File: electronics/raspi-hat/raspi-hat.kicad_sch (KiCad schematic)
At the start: 15 parts, among them J1 Raspberry Pi 40-Pin, J2 24V, J3 12V to other boards, J4 CAN, J5 5V to other boards, Q1 DMG2305UX-13, U1 MCP2515-xSO, U2 MAX33012EASA+, U3 DMMT5401-7-F, Y1 Crystal_GND24_Small

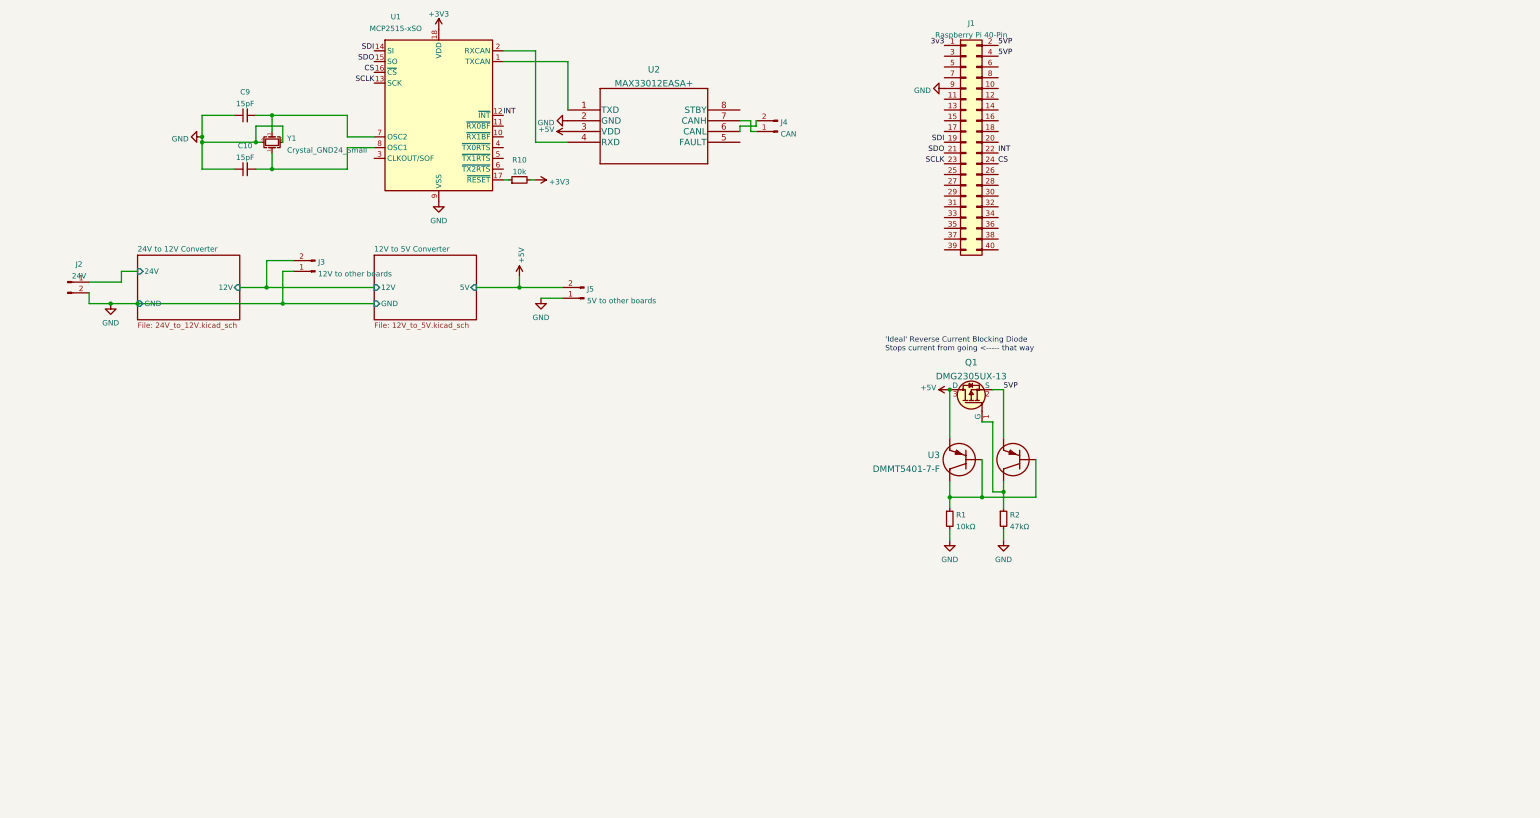
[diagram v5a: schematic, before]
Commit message: Finish designing raspi hat
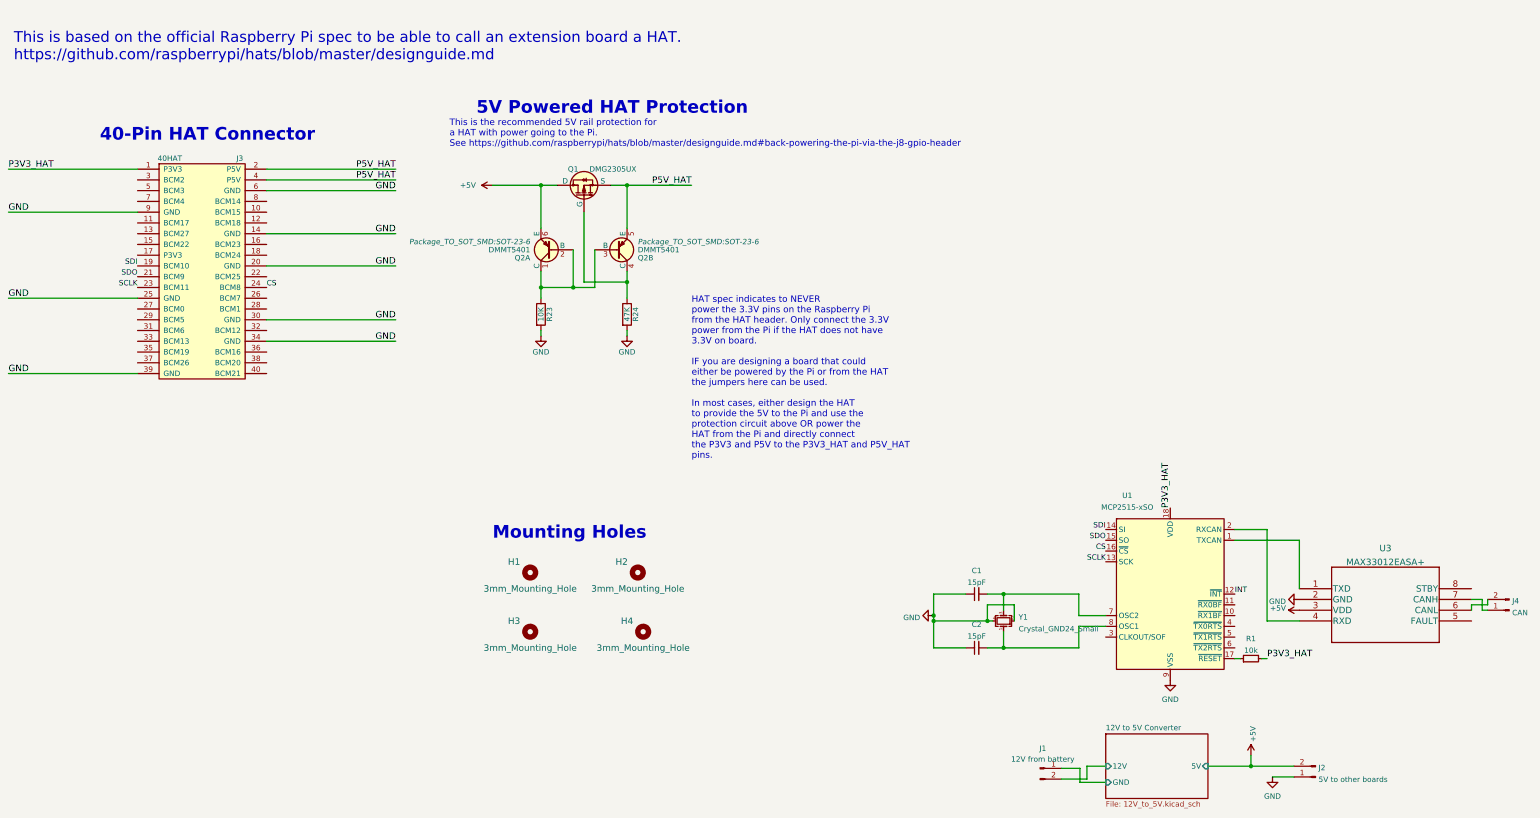
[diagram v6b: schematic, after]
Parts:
- removed C10, C9: 15pF, Capacitor_SMD:C_0603_1608Metric, symbol Device:C_Small
- removed J1: Raspberry Pi 40-Pin, Connector_PinHeader_2.54mm:PinHeader_2x20_P2.54mm_Vertical, symbol Connector_Generic:Conn_02x20_Odd_Even
- removed J3: 12V to other boards, Custom Footprints:PowerPoleThroughHole, symbol Connector:Conn_01x02_Male
- removed J5: 5V to other boards, Custom Footprints:LatchingConnector2POS, symbol Connector:Conn_01x02_Male
- removed Q1: DMG2305UX-13, digikey-footprints:SOT-23-3, symbol dk_Transistors-FETs-MOSFETs-Single:DMG2305UX-13
- removed R10: 10k, Resistor_SMD:R_0603_1608Metric, symbol Device:R_Small
- removed R2: 47kΩ, Resistor_SMD:R_0603_1608Metric, symbol Device:R_Small
- removed U2: MAX33012EASA+, MAX33012EASA+:MAX33012EASA+, symbol MAX33012EASA+:MAX33012EASA+
- removed U3: DMMT5401-7-F, DMMT5401-7-F:DMMT5401-7-F, symbol DMMT5401-7-F:DMMT5401-7-F
- added C1, C2: 15pF, Capacitor_SMD:C_0603_1608Metric, symbol Device:C_Small
- added H1, H2, H3, H4: 3mm_Mounting_Hole, project_footprints:NPTH_3mm_ID, symbol Mechanical:MountingHole
- added J1: 12V from battery, Custom Footprints:PowerPoleThroughHole, symbol Connector:Conn_01x02_Male
- added J3: 40HAT, Connector_PinSocket_2.54mm:PinSocket_2x20_P2.54mm_Vertical, symbol raspberrypi_hat:OX40HAT
- added Q1: DMG2305UX, Package_TO_SOT_SMD:SOT-23, symbol raspberrypi_hat:DMG2305UX
- added Q2: DMMT5401, Package_TO_SOT_SMD:SOT-23-6, symbol raspberrypi_hat:DMMT5401
- added R23: 10K, Resistor_SMD:R_0603_1608Metric_Pad0.84x1.00mm_HandSolder, symbol Device:R
- added R24: 47K, Resistor_SMD:R_0603_1608Metric_Pad0.84x1.00mm_HandSolder, symbol Device:R
- added U3: MAX33012EASA+, MAX33012EASA+:MAX33012EASA+, symbol MAX33012EASA+:MAX33012EASA+
- J2: value 24V -> 5V to other boards; footprint Custom Footprints:PowerPoleThroughHole -> Custom Footprints:LatchingConnector2POS
- R1: value 10kΩ -> 10k
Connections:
- net 24V to 12V Converter/24V is gone; now on net GND: J2.1 (Pin_1)
- net +5V: now also J2.2 (Pin_2), Q1.3 (D), Q2.6 (E), U3.3 (VDD)
- net 12V to 5V Converter/12V: now also J1.2 (Pin_2)
- net CS: now also J3.24 (BCM8)
- net GND: now also C1.1, C2.1, J3.14 (GND), J3.20 (GND), J3.25 (GND), J3.30 (GND), J3.34 (GND), J3.39 (GND), J3.6 (GND), J3.9 (GND), R23.2, R24.2, U3.2 (GND); no longer J2.2 (Pin_2), R1.2
- net SCLK: now also J3.23 (BCM11)
- net SDI: now also J3.19 (BCM10)
- net SDO: now also J3.21 (BCM9)
- net at U1.8 (OSC1), Y1.1: now also C2.2
- net at R1.1: now also U1.17 (~{RESET})
- net at U1.1 (TXCAN): now also U3.1 (TXD)
- net at U1.2 (RXCAN): now also U3.4 (RXD)
- net at U1.7 (OSC2), Y1.3: now also C1.2
- net at J4.2 (Pin_2): now also U3.6 (CANL)
- net at J4.1 (Pin_1): now also U3.7 (CANH)
- net +3V3 renamed P3V3_HAT
- net P3V3_HAT: now also R1.2, J3.1 (P3V3)
- new net: Q1.1 (G), Q2.4 (C), R24.1
- new net: Q2.1 (C), Q2.2 (B), Q2.3 (B), R23.1
- new net 12V to 5V Converter/GND: J1.1 (Pin_1)
- new net P5V_HAT: J3.2 (P5V), J3.4 (P5V), Q1.2 (S), Q2.5 (E)
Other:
- removed sheet 24V to 12V Converter
- note added: "40-Pin HAT Connector"
- note added: "5V Powered HAT Protection"
- note added: "HAT spec indicates to NEVER power the 3.3V pins on the Raspberry Pi from the HAT header. Only connect the 3.3V power from the Pi if the HAT does not have 3.3V on board. IF you are designing a board that could either be powered by the Pi or from the HAT the jumpers here can be used. In most cases, either design the HAT to provide the 5V to the Pi and use the protection circuit above OR power the H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"
- note added: "Mounting Holes"
- note added: "This is based on the official Raspberry Pi spec to be able to call an extension board a HAT. https://github.com/raspberrypi/hats/blob/master/designguide.md"
- note added: "This is the recommended 5V rail protection for a HAT with power going to the Pi. See https://github.com/raspberrypi/hats/blob/master/designguide.md#back-powering-the-pi-via-the-j8-gpio-header"
- note removed: "'Ideal' Reverse Current Blocking Diode Stops current from going <----- that way"
- title: (none) -> Raspberry Pi HAT

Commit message: Update raspi HAT schematic
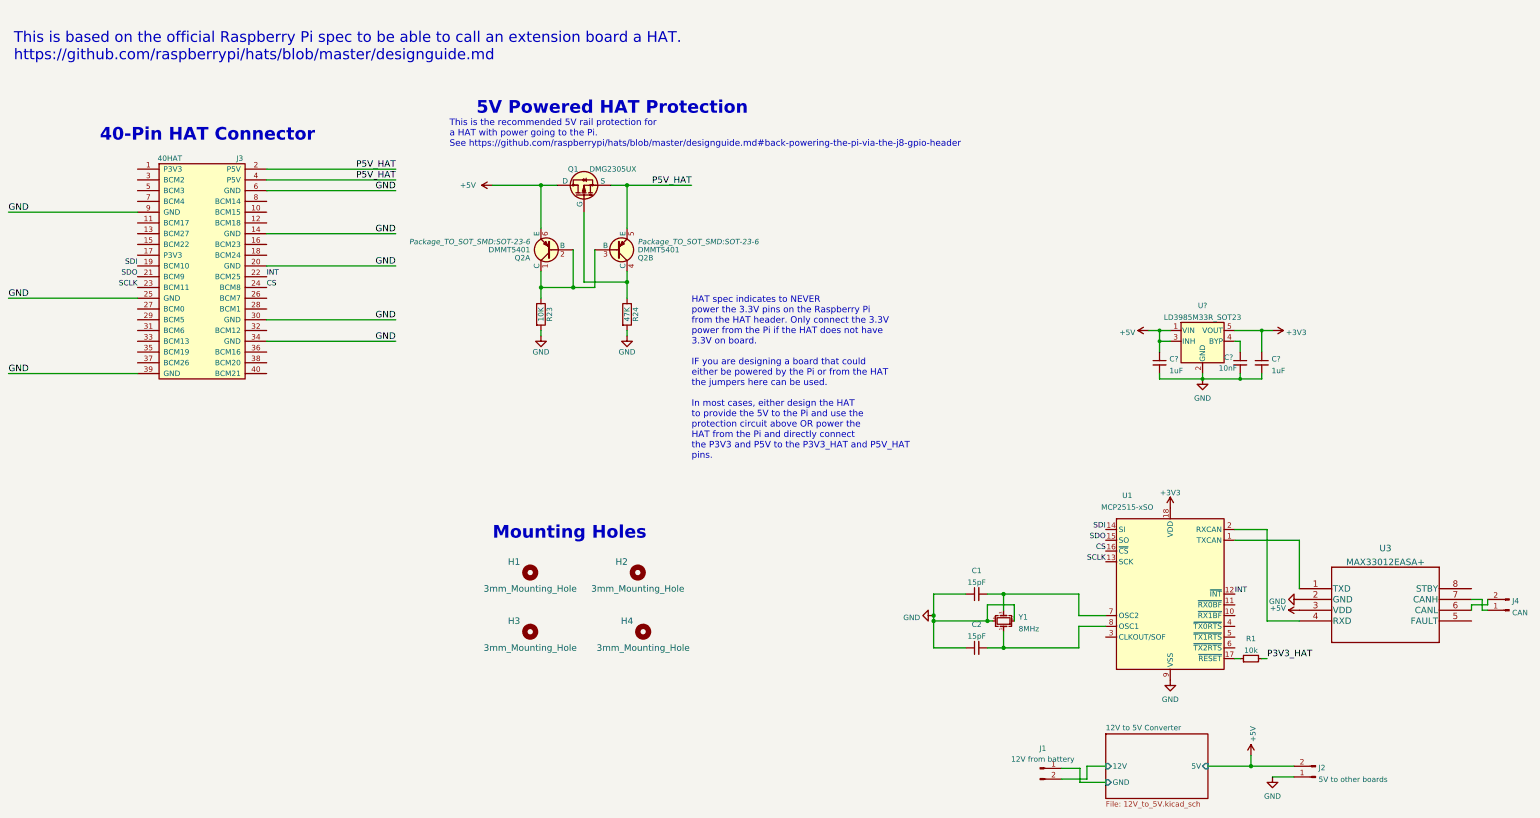
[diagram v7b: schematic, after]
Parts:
- added C? (x2): 1uF, symbol Device:C_Small
- added C?: 10nF, symbol Device:C_Small
- added U?: LD3985M33R_SOT23, Package_TO_SOT_SMD:SOT-23-5, symbol Regulator_Linear:LD3985M33R_SOT23
- Y1: value Crystal_GND24_Small -> 8MHz
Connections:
- net +5V: now also C?.1, U?.1 (VIN), U?.3 (INH)
- net GND: now also C?.2, C?.2, C?.2, U?.2 (GND)
- net INT: now also J3.22 (BCM25)
- net P3V3_HAT: no longer J3.1 (P3V3), U1.18 (VDD)
- new net: C?.1, U?.4 (BYP)
- new net +3V3: C?.1, U1.18 (VDD), U?.5 (VOUT)
